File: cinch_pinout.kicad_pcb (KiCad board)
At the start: 2 copper layers, 12.7 x 17.6 mm, 3 parts, among them J1 Conn, J2 Pinout

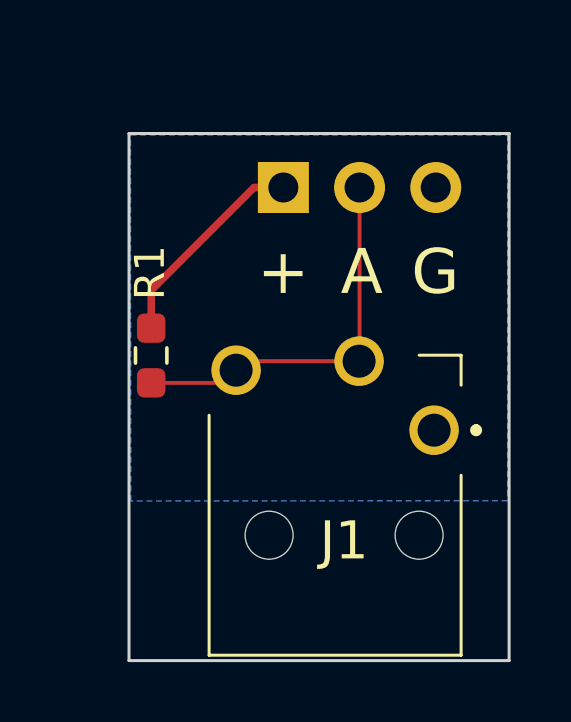
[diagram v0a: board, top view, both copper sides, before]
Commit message: Changed resistor footprint
Enables now both: SMD or throughhole resistor
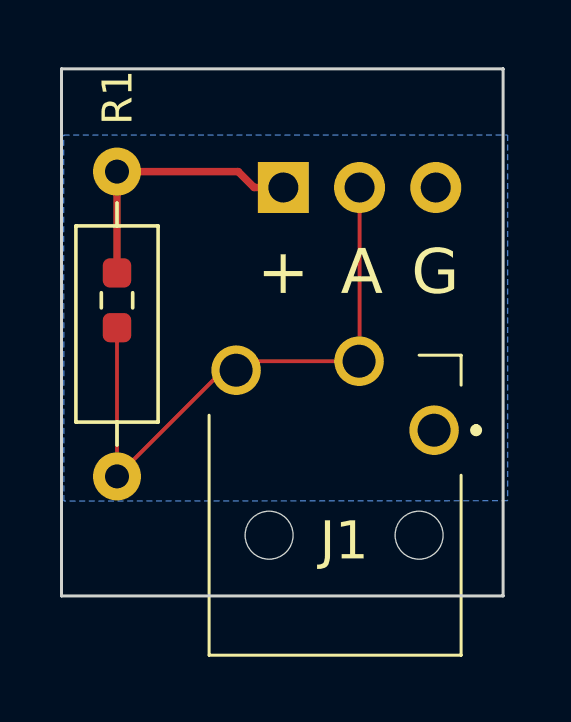
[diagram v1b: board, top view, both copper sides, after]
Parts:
- added R1T1: 1k, Resistor_THT:R_Axial_DIN0207_L6.3mm_D2.5mm_P10.16mm_Horizontal, F.Cu at (111.7, 73.8)
- moved R1 2.16 mm to (111.7, 78.1)
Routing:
- net AIN: track 13.0 -> 21.0 mm
- net +3V3: track 7.08 -> 9.14 mm
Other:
- board size 12.7 x 17.6 mm -> 14.7 x 17.6 mm
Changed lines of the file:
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@@
     (property "Mouser Part Number" "490-MJ-2509N")
     (property "Mouser Price/Stock" "https://www.mouser.co.uk/ProductDetail/CUI-Devices/MJ-2509N?qs=WyjlAZoYn53PDc56LTmBGw%3D%3D")
-    (property "Sheetfile" "ching_pinout.kicad_sch")
-    (property "Sheetname" "")
-    (attr through_hole exclude_from_pos_files exclude_from_bom)
+    (property "Sheetfile" "cinch_pinout.kicad_sch")
+    (property "Sheetname" "")
+    (attr through_hole exclude_from_pos_files)
     (fp_text reference "J1" (at 2 2.087) (layer "F.SilkS")
       (effects (font (size 1.27 1.27) (thickness 0.254)))
@@
   )
   (footprint "Resistor_SMD:R_0603_1608Metric_Pad0.98x0.95mm_HandSolder" (layer "F.Cu")
-    (at 112.85 79.91 -90)
+    (at 111.71 78.07 -90)
     (descr "Resistor SMD 0603 (1608 Metric), square (rectangular) end terminal, IPC_7351 nominal with elongated pad for handsoldering. (Body size source: IPC-SM-782 page 72, https://www.pcb-3d.com/wordpress/wp-content/uploads/ipc-sm-782a_amendment_1_and_2.pdf), generated with kicad-footprint-generator")
     (tags "resistor handsolder")
-    (property "Sheetfile" "ching_pinout.kicad_sch")
-    (property "Sheetname" "")
-    (attr smd exclude_from_pos_files exclude_from_bom)
-    (fp_text reference "R1" (at -2.76 0.04 90) (layer "F.SilkS")
-      (effects (font (size 1 1) (thickness 0.15)))
-    )
-    (fp_text value "1k" (at 2.66 0.04 90) (layer "F.Fab")
+    (property "Sheetfile" "cinch_pinout.kicad_sch")
+    (property "Sheetname" "")
+    (attr smd exclude_from_pos_files)
+    (fp_text reference "R1" (at -6.76 -0.02 90) (layer "F.SilkS")
+      (effects (font (size 1 1) (thickness 0.15)))
+    )
+    (fp_text value "1k" (at 8 0.04 90) (layer "F.Fab")
       (effects (font (size 1 1) (thickness 0.15)))
     )
@@
     )
   )
+  (footprint "Resistor_THT:R_Axial_DIN0207_L6.3mm_D2.5mm_P10.16mm_Horizontal" (layer "F.Cu")
+    (at 111.71 73.78 -90)
+    (descr "Resistor, Axial_DIN0207 series, Axial, Horizontal, pin pitch=10.16mm, 0.25W = 1/4W, length*diameter=6.3*2.5mm^2, http://cdn-reichelt.de/documents/datenblatt/B400/1_4W%23YAG.pdf")
+    (tags "Resistor Axial_DIN0207 series Axial Horizontal pin pitch 10.16mm 0.25W = 1/4W length 6.3mm diameter 2.5mm")
+    (property "Sheetfile" "cinch_pinout.kicad_sch")
+    (property "Sheetname" "")
+    (attr through_hole)
+    (fp_text reference "R1T1" (at 5.08 -2.37 90) (layer "F.SilkS") hide
+      (effects (font (size 1 1) (thickness 0.15)))
+    )
+    (fp_text value "1k" (at 5.08 2.37 90) (layer "F.Fab") hide
+      (effects (font (size 1 1) (thickness 0.15)))
+    )
+    (fp_text user "${REFERENCE}" (at 5.08 0 90) (layer "F.Fab") hide
+      (effects (font (size 1 1) (thickness 0.15)))
+    )
+    (fp_line (start 8.35 -1.37) (end 1.81 -1.37) (layer "F.SilkS") (width 0.12))
+    (fp_line (start 9.12 0) (end 8.35 0) (layer "F.SilkS") (width 0.12))
+    (fp_line (start 1.81 1.37) (end 8.35 1.37) (layer "F.SilkS") (width 0.12))
+    (fp_line (start 8.35 1.37) (end 8.35 -1.37) (layer "F.SilkS") (width 0.12))
+    (fp_line (start 1.04 0) (end 1.81 0) (layer "F.SilkS") (width 0.12))
+    (fp_line (start 1.81 -1.37) (end 1.81 1.37) (layer "F.SilkS") (width 0.12))
+    (fp_line (start 11.21 -1.5) (end -1.05 -1.5) (layer "F.CrtYd") (width 0.05))
+    (fp_line (start 11.21 1.5) (end 11.21 -1.5) (layer "F.CrtYd") (width 0.05))
+    (fp_line (start -1.05 -1.5) (end -1.05 1.5) (layer "F.CrtYd") (width 0.05))
+    (fp_line (start -1.05 1.5) (end 11.21 1.5) (layer "F.CrtYd") (width 0.05))
+    (fp_line (start 0 0) (end 1.93 0) (layer "F.Fab") (width 0.1))
+    (fp_line (start 1.93 -1.25) (end 1.93 1.25) (layer "F.Fab") (width 0.1))
+    (fp_line (start 10.16 0) (end 8.23 0) (layer "F.Fab") (width 0.1))
+    (fp_line (start 8.23 1.25) (end 8.23 -1.25) (layer "F.Fab") (width 0.1))
+    (fp_line (start 1.93 1.25) (end 8.23 1.25) (layer "F.Fab") (width 0.1))
+    (fp_line (start 8.23 -1.25) (end 1.93 -1.25) (layer "F.Fab") (width 0.1))
+    (pad "1" thru_hole circle (at 0 0 270) (size 1.6 1.6) (drill 0.8) (layers *.Cu *.Mask)
+      (net 3 "+3V3") (pintype "passive"))
+    (pad "2" thru_hole oval (at 10.16 0 270) (size 1.6 1.6) (drill 0.8) (layers *.Cu *.Mask)
+      (net 2 "AIN") (pintype "passive"))
+    (model "${KICAD6_3DMODEL_DIR}/Resistor_THT.3dshapes/R_Axial_DIN0207_L6.3mm_D2.5mm_P10.16mm_Horizontal.wrl"
+      (offset (xyz 0 0 0))
+      (scale (xyz 1 1 1))
+      (rotate (xyz 0 0 0))
+    )
+  )
   (footprint "Connector_PinHeader_2.54mm:PinHeader_1x03_P2.54mm_Vertical" (layer "B.Cu")
     (at 117.255 74.31 -90)
     (descr "Through hole straight pin header, 1x03, 2.54mm pitch, single row")
     (tags "Through hole pin header THT 1x03 2.54mm single row")
-    (property "Sheetfile" "ching_pinout.kicad_sch")
-    (property "Sheetname" "")
-    (attr through_hole exclude_from_pos_files exclude_from_bom)
+    (property "Sheetfile" "cinch_pinout.kicad_sch")
+    (property "Sheetname" "")
+    (attr through_hole exclude_from_pos_files)
     (fp_text reference "J2" (at 0 2.33 90) (layer "B.SilkS")
       (effects (font (size 1 1) (thickness 0.15)) (justify mirror))
@@
     )
   )
-  (gr_rect (start 112.11 72.51) (end 124.78 90.08) (layer "Edge.Cuts") (width 0.1) (fill none))
+  (gr_rect (start 109.86 70.355) (end 124.58 87.925) (layer "Edge.Cuts") (width 0.1) (fill none))
   (gr_text "G" (at 122.32 77.13) (layer "F.SilkS")
     (effects (font (size 1.5 1.5) (thickness 0.3)))
@@
   (segment (start 115.68 80.4) (end 115.2575 80.8225) (width 0.13) (layer "F.Cu") (net 2))
   (segment (start 119.795 74.31) (end 119.795 80.085) (width 0.13) (layer "F.Cu") (net 2))
-  (segment (start 115.2575 80.8225) (end 112.85 80.8225) (width 0.13) (layer "F.Cu") (net 2))
+  (segment (start 111.71 83.94) (end 111.71 78.9825) (width 0.13) (layer "F.Cu") (net 2))
+  (segment (start 111.71 83.94) (end 115.25 80.4) (width 0.13) (layer "F.Cu") (net 2))
   (segment (start 119.78 80.1) (end 115.98 80.1) (width 0.13) (layer "F.Cu") (net 2))
   (segment (start 119.795 80.085) (end 119.78 80.1) (width 0.13) (layer "F.Cu") (net 2))
+  (segment (start 115.25 80.4) (end 115.68 80.4) (width 0.13) (layer "F.Cu") (net 2))
   (segment (start 117.255 74.31) (end 116.28 74.31) (width 0.25) (layer "F.Cu") (net 3))
-  (segment (start 116.28 74.31) (end 112.85 77.74) (width 0.25) (layer "F.Cu") (net 3))
-  (segment (start 112.85 77.74) (end 112.85 78.9975) (width 0.25) (layer "F.Cu") (net 3))
+  (segment (start 115.75 73.78) (end 111.71 73.78) (width 0.25) (layer "F.Cu") (net 3))
+  (segment (start 116.28 74.31) (end 115.75 73.78) (width 0.25) (layer "F.Cu") (net 3))
+  (segment (start 111.71 73.78) (end 111.71 77.1575) (width 0.25) (layer "F.Cu") (net 3))
   (zone (net 1) (net_name "GND") (layer "B.Cu") (hatch edge 0.508)
     (connect_pads (clearance 0.508))
     (min_thickness 0.254) (filled_areas_thickness no)
-    (fill yes (thermal_gap 0.508) (thermal_bridge_width 0.508))
+    (fill (thermal_gap 0.508) (thermal_bridge_width 0.508))
     (polygon
       (pts
         (xy 124.73 84.75)
-        (xy 112.17 84.76)
-        (xy 112.16 72.56)
+        (xy 109.93993 84.761829)
+        (xy 109.92993 72.561829)
         (xy 124.73 72.56)
       )
